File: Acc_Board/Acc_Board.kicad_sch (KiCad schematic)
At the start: 43 parts, among them J1 1053091202, J10 1053091202, J2 1053091202, J3 1053091202, J4 1053091202, J5 1053091202, J6 1053091202, J8 1053091202, J9 1053091202, K1 Relay_SPST-NO, U1 ISO1050DUB, U13 R-78B5.0-2.0, U2 NUCLEO-L432KC, U4 PQDE6W-Q110-S5-H-D

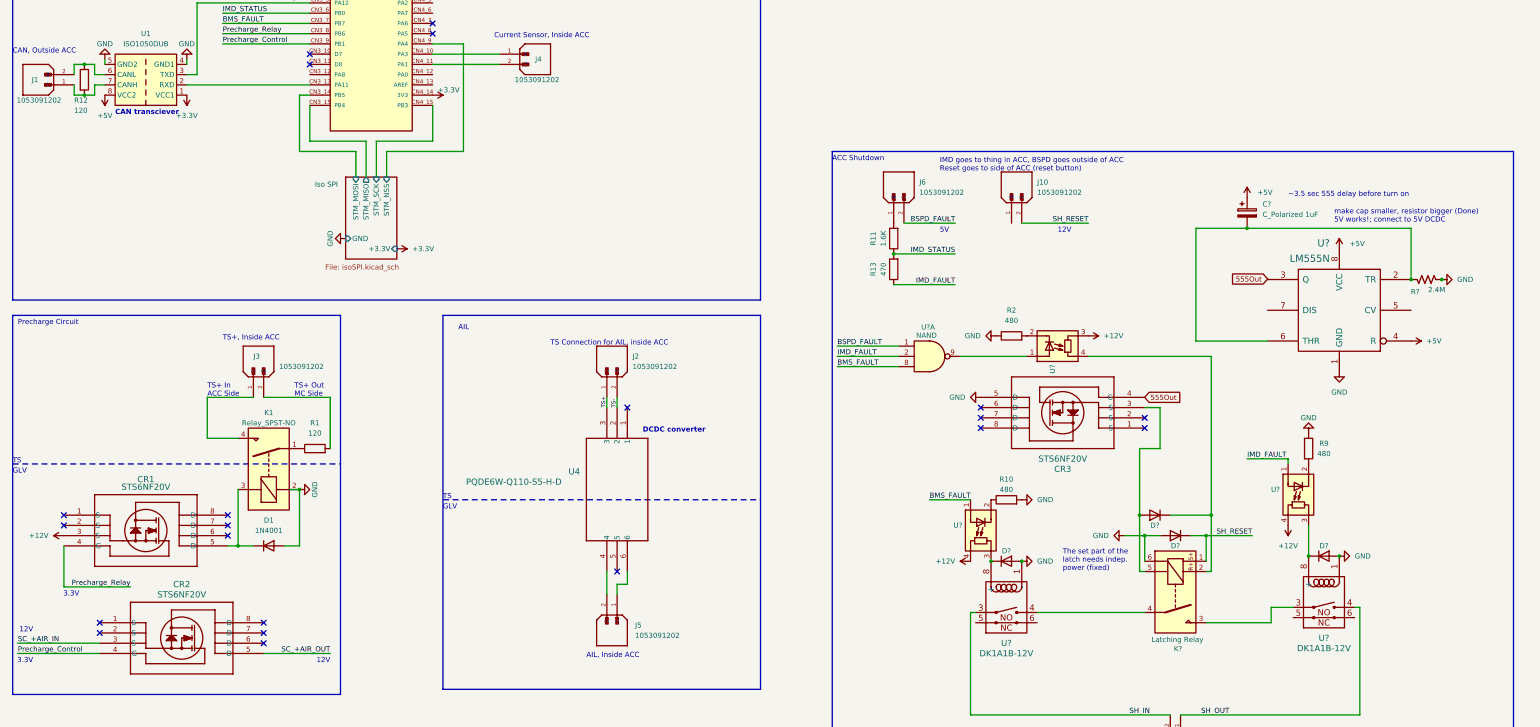
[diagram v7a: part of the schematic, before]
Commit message: Cleaned up resistors on Acc board
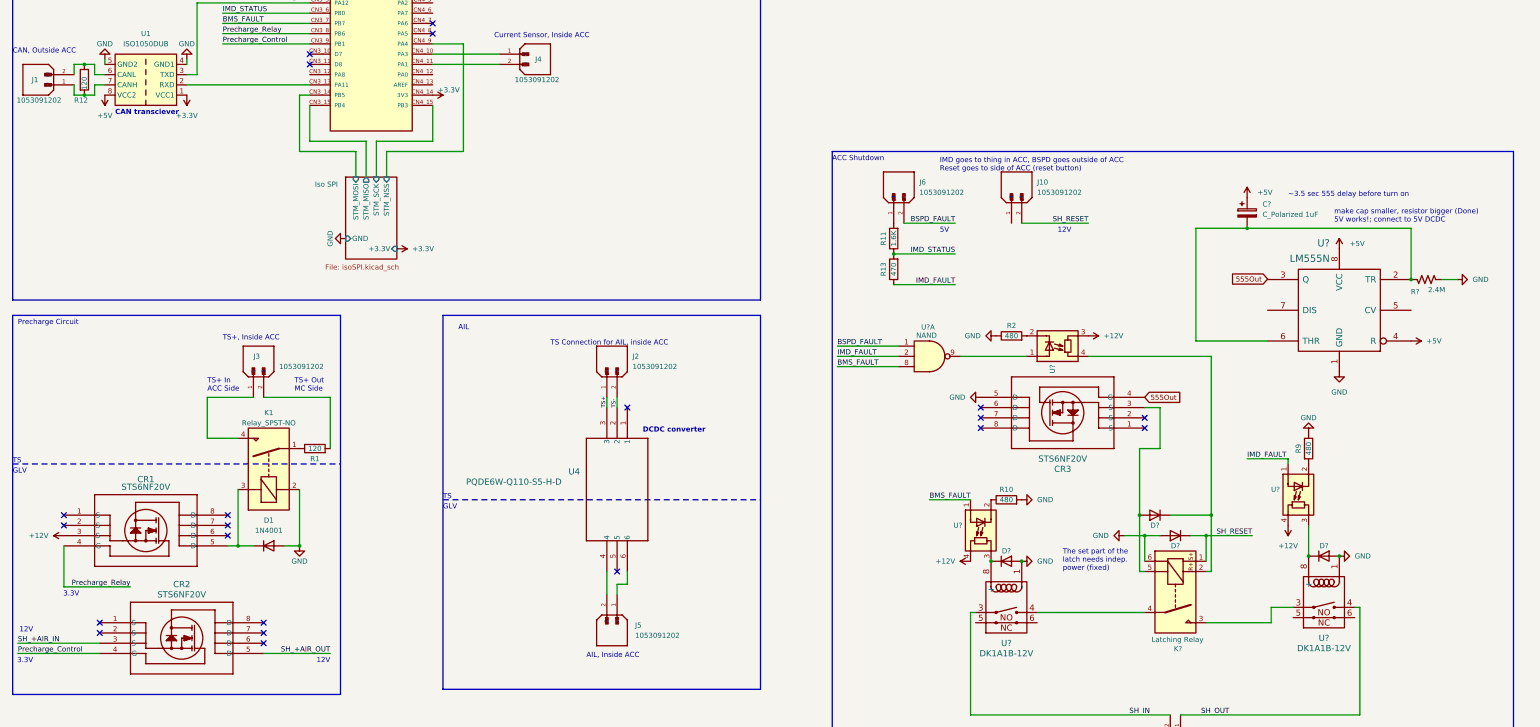
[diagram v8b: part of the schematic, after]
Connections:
- net SC_+AIR_IN renamed SH_+AIR_IN
- net SC_+AIR_OUT renamed SH_+AIR_OUT
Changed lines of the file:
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@@
   (junction (at 127 247.65) (diameter 0) (color 0 0 0 0)
   )
-  (junction (at 377.19 106.68) (diameter 0) (color 0 0 0 0)
-  )
   (junction (at 303.53 170.18) (diameter 0) (color 0 0 0 0)
   )
@@
   (junction (at 302.26 165.1) (diameter 0) (color 0 0 0 0)
   )
+  (junction (at 93.98 172.72) (diameter 0) (color 0 0 0 0)
+  )
   (junction (at 273.05 176.53) (diameter 0) (color 0 0 0 0)
   )
   (junction (at 162.56 240.03) (diameter 0) (color 0 0 0 0)
-  )
-  (junction (at 93.98 158.75) (diameter 0) (color 0 0 0 0)
   )
   (junction (at 151.13 240.03) (diameter 0) (color 0 0 0 0)
@@
   )
   (wire (pts (xy 82.55 135.89) (xy 71.12 135.89))
-    (stroke (width 0) (type default))
+    (stroke (width 1) (type default))
   )
   (wire (pts (xy 276.86 189.23) (xy 303.53 189.23))
@@
   )
   (wire (pts (xy 71.12 146.05) (xy 78.74 146.05))
-    (stroke (width 0) (type default))
+    (stroke (width 1) (type default))
   )
   (wire (pts (xy 35.56 182.88) (xy 35.56 172.72))
@@
   )
   (wire (pts (xy 85.09 135.89) (xy 101.6 135.89))
-    (stroke (width 0) (type default))
+    (stroke (width 1) (type default))
   )
   (wire (pts (xy 115.57 74.93) (xy 134.62 74.93))
@@
     (stroke (width 0) (type default))
   )
-  (wire (pts (xy 377.19 106.68) (xy 377.19 106.553))
-    (stroke (width 0) (type default))
-  )
   (wire (pts (xy 318.77 170.18) (xy 314.96 170.18))
     (stroke (width 0) (type default))
@@
   )
   (wire (pts (xy 256.54 92.71) (xy 243.84 92.71))
+    (stroke (width 0) (type default))
+  )
+  (wire (pts (xy 377.19 106.68) (xy 381 106.68))
     (stroke (width 0) (type default))
   )
@@
   )
   (wire (pts (xy 101.6 135.89) (xy 101.6 148.59))
-    (stroke (width 0) (type default))
+    (stroke (width 1) (type default))
   )
   (wire (pts (xy 307.34 148.59) (xy 307.34 138.43))
@@
     (stroke (width 0) (type default))
   )
-  (wire (pts (xy 93.98 158.75) (xy 91.44 158.75))
-    (stroke (width 0) (type default))
-  )
   (wire (pts (xy 115.57 240.03) (xy 127 240.03))
     (stroke (width 0) (type default))
@@
   )
   (wire (pts (xy 71.12 135.89) (xy 71.12 146.05))
-    (stroke (width 0) (type default))
+    (stroke (width 1) (type default))
   )
   (wire (pts (xy 302.26 165.1) (xy 302.26 179.07))
@@
     (fill (type none))
   )
-  (text "TS+ In\nACC Side" (at 71.12 135.89 0)
+  (text "TS+ In\nACC Side" (at 71.12 134.62 0)
     (effects (font (size 1.27 1.27)) (justify left bottom))
   )
@@
     (effects (font (size 1.27 1.27)) (justify left bottom))
   )
-  (text "TS+ Out\nMC Side" (at 92.71 135.89 0)
+  (text "TS+ Out\nMC Side" (at 92.71 134.62 0)
     (effects (font (size 1.27 1.27)) (justify left bottom))
   )
@@
     (effects (font (size 1.27 1.27)) (justify right bottom))
   )
-  (label "SC_+AIR_IN" (at 24.13 196.85 0) (fields_autoplaced)
-    (effects (font (size 1.27 1.27)) (justify left bottom))
-  )
-  (label "SC_+AIR_OUT" (at 101.6 199.39 180) (fields_autoplaced)
+  (label "SH_+AIR_IN" (at 24.13 196.85 0) (fields_autoplaced)
+    (effects (font (size 1.27 1.27)) (justify left bottom))
+  )
+  (label "SH_+AIR_OUT" (at 101.6 199.39 180) (fields_autoplaced)
     (effects (font (size 1.27 1.27)) (justify right bottom))
   )
@@
   )
   (symbol (lib_id "Device:R") (at 97.79 148.59 90) (unit 1)
-    (in_bom yes) (on_board yes) (dnp no) (fields_autoplaced)
-    (property "Reference" "R1" (at 97.79 142.24 90)
-      (effects (font (size 1.27 1.27)))
-    )
-    (property "Value" "120" (at 97.79 144.78 90)
+    (in_bom yes) (on_board yes) (dnp no)
+    (property "Reference" "R1" (at 97.79 151.13 90)
+      (effects (font (size 1.27 1.27)))
+    )
+    (property "Value" "120" (at 97.79 148.59 90)
       (effects (font (size 1.27 1.27)))
     )
@@
   (symbol (lib_name "R_2") (lib_id "Device:R") (at 241.3 96.52 180) (unit 1)
     (in_bom yes) (on_board yes) (dnp no)
-    (property "Reference" "R11" (at 236.22 96.52 90)
-      (effects (font (size 1.27 1.27)))
-    )
-    (property "Value" "1.6K" (at 238.76 96.52 90)
+    (property "Reference" "R11" (at 238.76 96.52 90)
+      (effects (font (size 1.27 1.27)))
+    )
+    (property "Value" "1.6K" (at 241.3 96.52 90)
       (effects (font (size 1.27 1.27)))
     )
@@
       (effects (font (size 1.27 1.27)) (justify left))
     )
-    (property "Value" "120" (at 38.1 64.77 0)
+    (property "Value" "120" (at 40.64 59.69 90)
       (effects (font (size 1.27 1.27)) (justify left))
     )
@@
   (symbol (lib_name "R_2") (lib_id "Device:R") (at 241.3 104.14 180) (unit 1)
     (in_bom yes) (on_board yes) (dnp no)
-    (property "Reference" "R13" (at 236.22 104.14 90)
-      (effects (font (size 1.27 1.27)))
-    )
-    (property "Value" "470" (at 238.76 104.14 90)
+    (property "Reference" "R13" (at 238.76 104.14 90)
+      (effects (font (size 1.27 1.27)))
+    )
+    (property "Value" "470" (at 241.3 104.14 90)
       (effects (font (size 1.27 1.27)))
     )
@@
   (symbol (lib_name "R_1") (lib_id "Device:R") (at 344.17 148.59 0) (unit 1)
     (in_bom yes) (on_board yes) (dnp no)
-    (property "Reference" "R9" (at 347.98 147.32 0)
-      (effects (font (size 1.27 1.27)))
-    )
-    (property "Value" "480" (at 347.98 149.86 0)
+    (property "Reference" "R9" (at 341.63 148.59 90)
+      (effects (font (size 1.27 1.27)))
+    )
+    (property "Value" "480" (at 344.17 148.59 90)
       (effects (font (size 1.27 1.27)))
     )
@@
   (symbol (lib_name "R_1") (lib_id "Device:R") (at 269.24 161.29 90) (unit 1)
     (in_bom yes) (on_board yes) (dnp no)
-    (property "Reference" "R10" (at 269.24 156.21 90)
-      (effects (font (size 1.27 1.27)))
-    )
-    (property "Value" "480" (at 269.24 158.75 90)
+    (property "Reference" "R10" (at 269.24 158.75 90)
+      (effects (font (size 1.27 1.27)))
+    )
+    (property "Value" "480" (at 269.24 161.29 90)
       (effects (font (size 1.27 1.27)))
     )
@@
     )
   )
-  (symbol (lib_id "power:GND") (at 93.98 158.75 90) (unit 1)
-    (in_bom yes) (on_board yes) (dnp no)
-    (property "Reference" "#PWR07" (at 100.33 158.75 0)
-      (effects (font (size 1.27 1.27)) hide)
-    )
-    (property "Value" "GND" (at 97.79 158.75 0)
-      (effects (font (size 1.27 1.27)))
-    )
-    (property "Footprint" "" (at 93.98 158.75 0)
-      (effects (font (size 1.27 1.27)) hide)
-    )
-    (property "Datasheet" "" (at 93.98 158.75 0)
+  (symbol (lib_id "power:GND") (at 93.98 172.72 0) (unit 1)
+    (in_bom yes) (on_board yes) (dnp no)
+    (property "Reference" "#PWR07" (at 93.98 179.07 0)
+      (effects (font (size 1.27 1.27)) hide)
+    )
+    (property "Value" "GND" (at 93.98 176.53 0)
+      (effects (font (size 1.27 1.27)))
+    )
+    (property "Footprint" "" (at 93.98 172.72 0)
+      (effects (font (size 1.27 1.27)) hide)
+    )
+    (property "Datasheet" "" (at 93.98 172.72 0)
       (effects (font (size 1.27 1.27)) hide)
     )
@@
     )
   )
-  (symbol (lib_id "power:GND") (at 377.19 106.68 90) (unit 1)
-    (in_bom yes) (on_board yes) (dnp no) (fields_autoplaced)
-    (property "Reference" "#PWR027" (at 383.54 106.68 0)
-      (effects (font (size 1.27 1.27)) hide)
-    )
-    (property "Value" "GND" (at 381 106.68 90)
+  (symbol (lib_id "power:GND") (at 381 106.68 90) (unit 1)
+    (in_bom yes) (on_board yes) (dnp no) (fields_autoplaced)
+    (property "Reference" "#PWR027" (at 387.35 106.68 0)
+      (effects (font (size 1.27 1.27)) hide)
+    )
+    (property "Value" "GND" (at 384.81 106.68 90)
       (effects (font (size 1.27 1.27)) (justify right))
     )
-    (property "Footprint" "" (at 377.19 106.68 0)
-      (effects (font (size 1.27 1.27)) hide)
-    )
-    (property "Datasheet" "" (at 377.19 106.68 0)
+    (property "Footprint" "" (at 381 106.68 0)
+      (effects (font (size 1.27 1.27)) hide)
+    )
+    (property "Datasheet" "" (at 381 106.68 0)
       (effects (font (size 1.27 1.27)) hide)
     )
@@
   )
   (symbol (lib_name "R_1") (lib_id "Device:R") (at 270.51 120.65 90) (unit 1)
-    (in_bom yes) (on_board yes) (dnp no) (fields_autoplaced)
-    (property "Reference" "R2" (at 270.51 114.3 90)
-      (effects (font (size 1.27 1.27)))
-    )
-    (property "Value" "480" (at 270.51 116.84 90)
-      (effects (font (size 1.27 1.27)))
-    )
+    (in_bom yes) (on_board yes) (dnp no)
+    (property "Reference" "R2" (at 270.51 118.11 90)
+      (effects (font (size 1.27 1.27)))
+    )
+    (property "Value" "480" (at 270.51 120.65 90)
+      (effects (font (size 1.27 1.27)))
+    )
